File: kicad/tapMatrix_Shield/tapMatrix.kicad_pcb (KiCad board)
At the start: 2 copper layers, 68.6 x 53.3 mm, 29 parts, among them P5 TS_ZIF, P6 LED_MATRIX_HDR, U1 MCP1700T-3302E/MB, U2 MCP4921-E/SN, U3 74LS125, U4 TL072, U5 SD_CARD, U6 DS1307

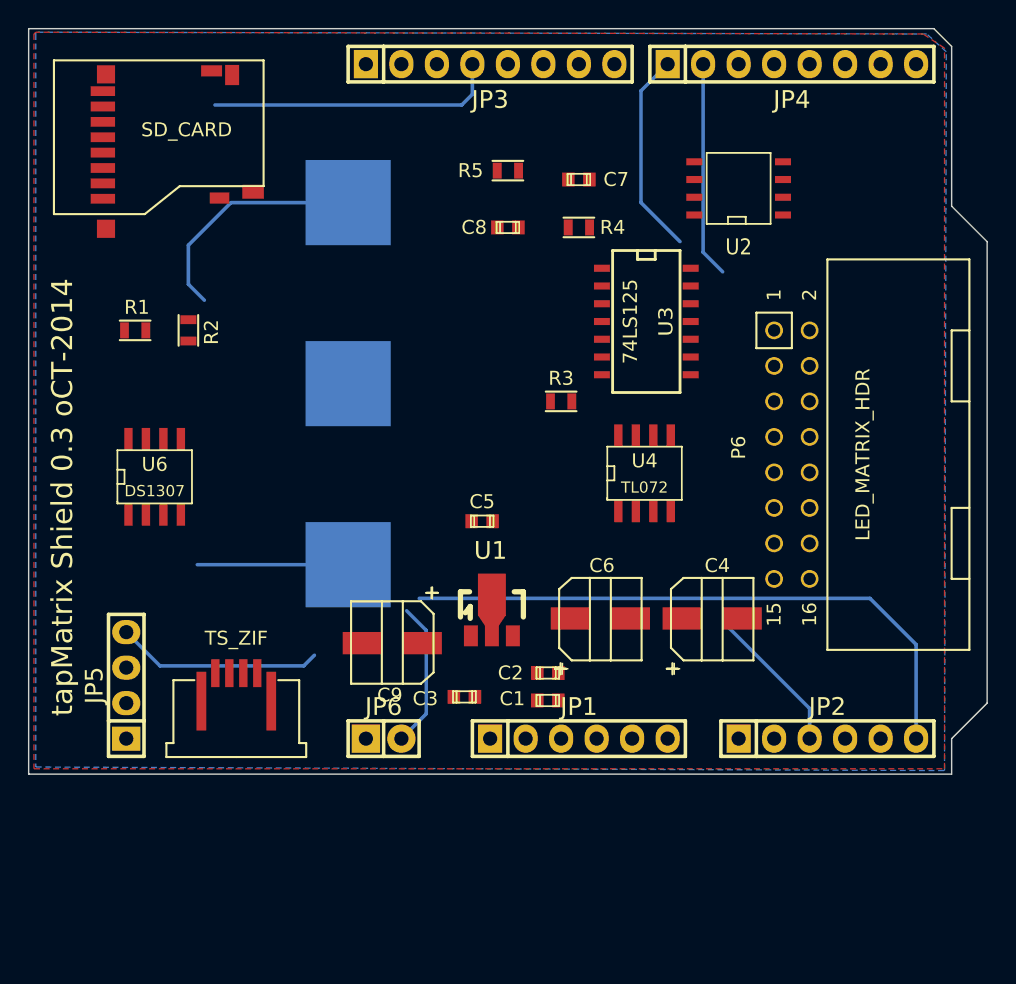
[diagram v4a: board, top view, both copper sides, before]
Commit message: catch up with commits for moving R and C to tapmatrix library
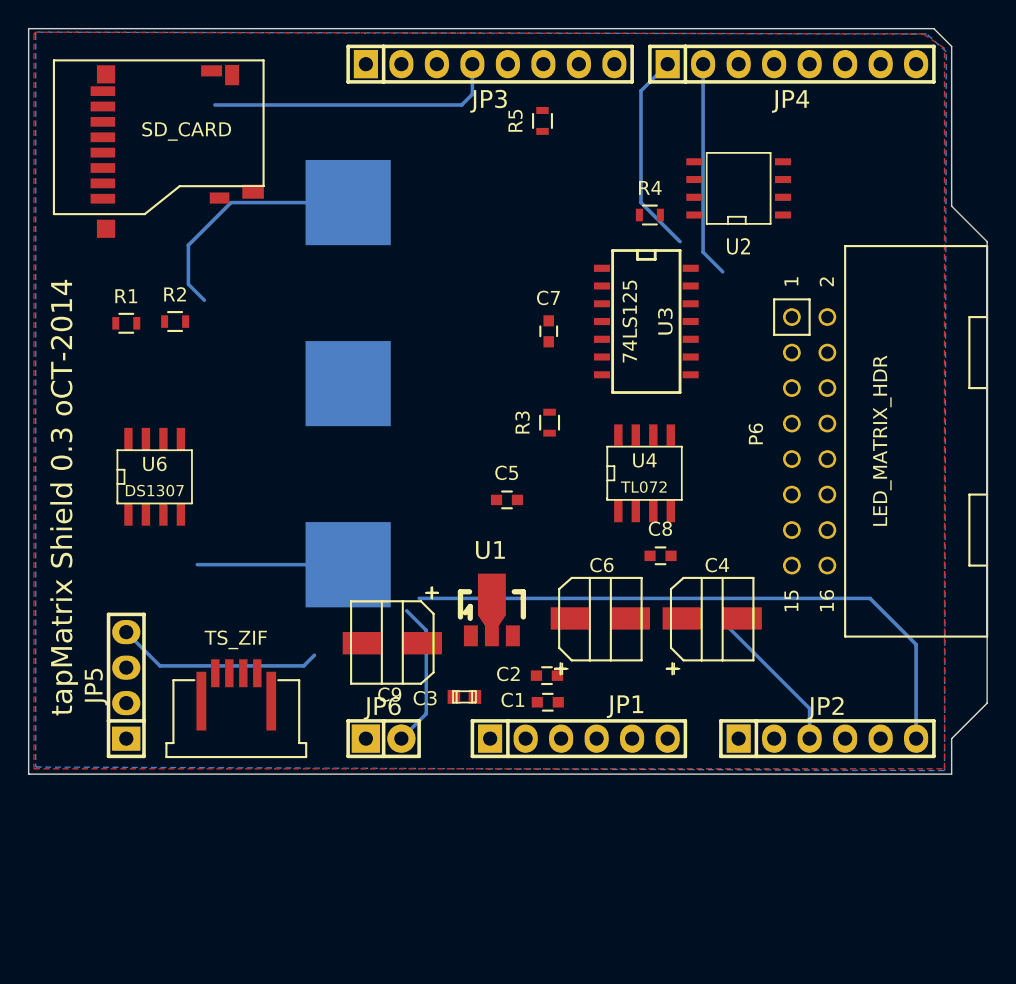
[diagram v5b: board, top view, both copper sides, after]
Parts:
- C1, C2, C5, C7, C8: footprint Capacitors_SMD:c_0603 -> tapmatrix:C_0603
- R1, R2, R3, R4, R5: footprint Resistors_SMD:R_0603 -> tapmatrix:R_0603
- moved C8 25.9 mm to (176.0, 124.1)
- moved C7 11.1 mm to (168.0, 108.0), turned to 270 degrees
- moved R4 5.16 mm to (175.3, 99.7)
- moved R5 4.33 mm to (167.6, 93.0), turned to 90 degrees
- moved C5 2.34 mm to (165.0, 120.1)
- moved R3 1.73 mm to (168.1, 114.6), turned to 90 degrees
- moved P6 1.59 mm to (186.7, 115.9)
- moved R2 1.14 mm to (141.3, 107.3), turned to 0 degrees
- moved R1 0.81 mm to (137.8, 107.4)
- moved C2 0.20 mm to (167.9, 132.7), turned to 180 degrees
- moved C1 0.13 mm to (168.0, 134.6), turned to 180 degrees

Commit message: move pin header footprints to tapmatrix library
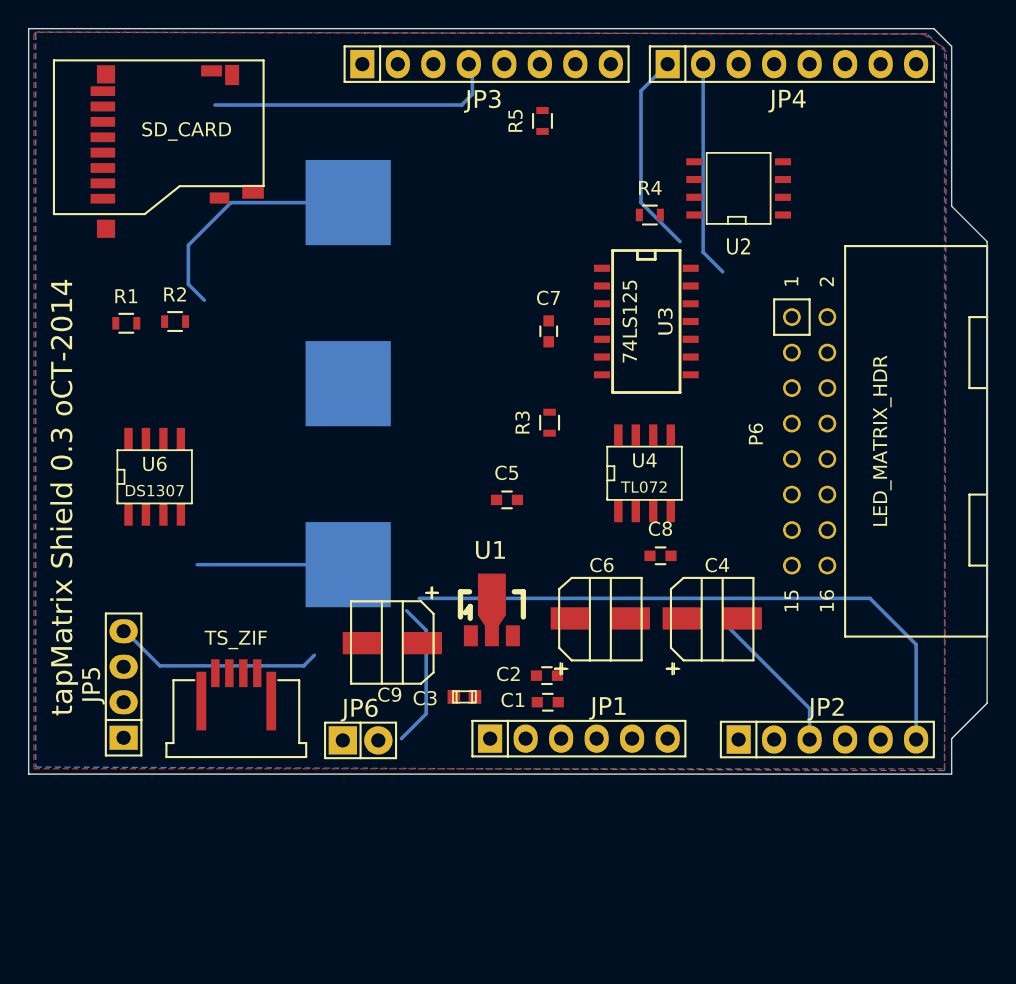
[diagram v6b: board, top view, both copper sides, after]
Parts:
- JP1, JP2: footprint Pin_Headers:Pin_Header_Straight_1x06 -> tapmatrix:Pin_Header_Straight_1x06
- JP3, JP4: footprint Pin_Headers:Pin_Header_Straight_1x08 -> tapmatrix:Pin_Header_Straight_1x08
- JP5: footprint Pin_Headers:Pin_Header_Straight_1x04 -> tapmatrix:Pin_Header_Straight_1x04
- JP6: footprint Pin_Headers:Pin_Header_Straight_1x02 -> tapmatrix:Pin_Header_Straight_1x02
- moved JP6 1.66 mm to (154.6, 137.3)
- moved JP3 0.25 mm to (163.6, 88.9)
- moved JP5 0.20 mm to (137.6, 133.3)
- moved JP2 0.06 mm to (188.0, 137.2)
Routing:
- net Net-(C9-Pad2): track 10.5 -> 0.00 mm
- net (no net): track 0.00 -> 10.5 mm

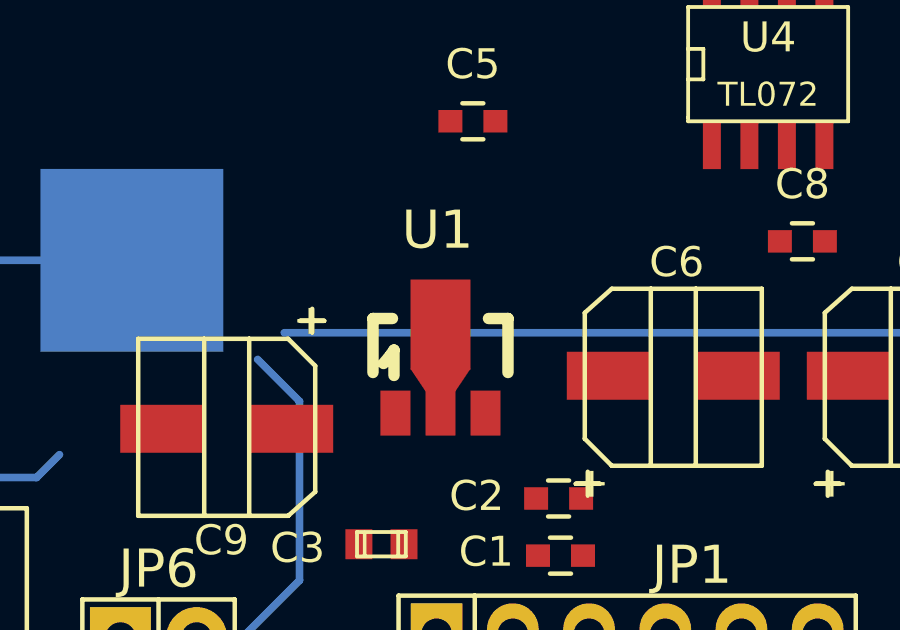
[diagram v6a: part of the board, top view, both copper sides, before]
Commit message: move SOT-89-3 footprint to tapmatrix library
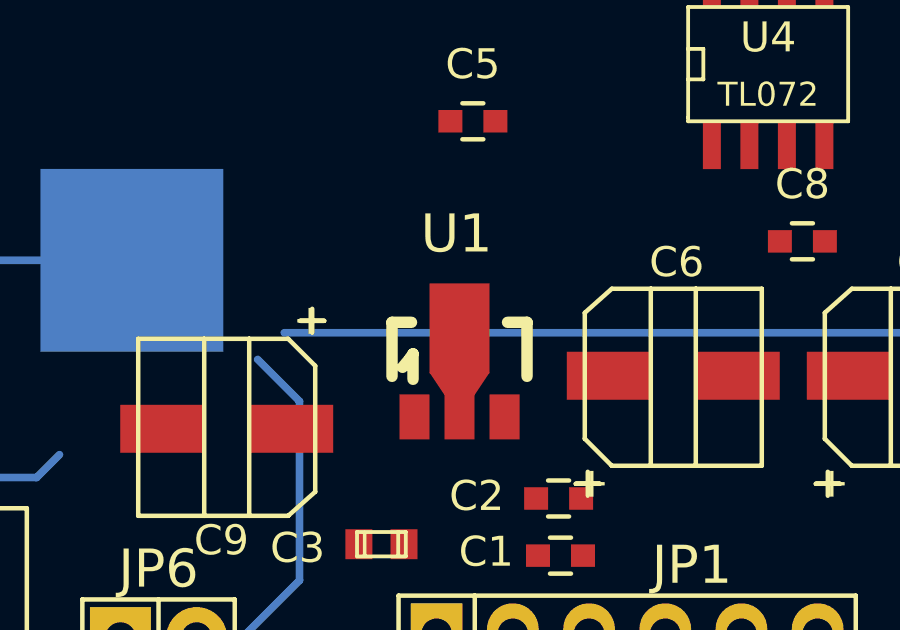
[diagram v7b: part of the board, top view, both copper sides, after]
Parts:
- U1: footprint Housings_SOT-89:SOT89-3_Housing -> tapmatrix:SOT89-3_Housing
- moved U1 0.65 mm to (164.6, 128.1)
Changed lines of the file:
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@@
-    )
-  )
-  (module Housings_SOT-89:SOT89-3_Housing (layer F.Cu)
-    (at 163.957 127.9525)
-    (descr "SOT89-3, Housing,")
-    (tags "SOT89-3, Housing,")
-    (attr smd)
-    (fp_text reference U1 (at -0.09906 -4.24942) (layer F.SilkS)
-      (effects (font (thickness 0.3048)))
-    )
-    (fp_text value MCP1700T-3302E/MB (at -0.20066 4.59994) (layer F.SilkS) hide
-      (effects (font (thickness 0.3048)))
-    )
-    (fp_line (start -1.89992 0.20066) (end -1.651 -0.09906) (layer F.SilkS) (width 0.381))
-    (fp_line (start -1.651 -0.09906) (end -1.5494 -0.24892) (layer F.SilkS) (width 0.381))
-    (fp_line (start -1.5494 -0.24892) (end -1.5494 0.59944) (layer F.SilkS) (width 0.381))
-    (fp_line (start -2.25044 -1.30048) (end -2.25044 0.50038) (layer F.SilkS) (width 0.381))
-    (fp_line (start -2.25044 -1.30048) (end -1.6002 -1.30048) (layer F.SilkS) (width 0.381))
-    (fp_line (start 2.25044 -1.30048) (end 2.25044 0.50038) (layer F.SilkS) (width 0.381))
-    (fp_line (start 2.25044 -1.30048) (end 1.6002 -1.30048) (layer F.SilkS) (width 0.381))
-    (pad 1 smd rect (at -1.50114 1.85166) (size 1.00076 1.50114) (layers F.Cu F.Paste F.Mask)
-      (net 2 GND))
-    (pad 2 smd rect (at 0 1.85166) (size 1.00076 1.50114) (layers F.Cu F.Paste F.Mask)
-      (net 46 +3.3V))
-    (pad 3 smd rect (at 1.50114 1.85166) (size 1.00076 1.50114) (layers F.Cu F.Paste F.Mask)
-      (net 1 +5V))
-    (pad 2 smd rect (at 0 -1.09982) (size 1.99898 2.99974) (layers F.Cu F.Paste F.Mask)
-      (net 46 +3.3V))
-    (pad 2 smd trapezoid (at 0 0.7493 180) (size 1.50114 0.7493) (rect_delta 0 0.50038 ) (layers F.Cu F.Paste F.Mask)
-      (net 46 +3.3V))
-    (model SOT89-3_SOT89-5_Housing_Wings3d_RevA_02Sep2012/SOT89-3_Housing_Faktor03937_RevA_02Sep2012.wrl
-      (at (xyz 0 0 0))
-      (scale (xyz 0.3937000036239624 0.3937000036239624 0.3937000036239624))
-      (rotate (xyz 0 0 0))
     )
   )
@@
       (rotate (xyz 0 0 0))
     )
+  )
+  (module tapmatrix:SOT89-3_Housing (layer F.Cu)
+    (at 164.592 128.0795)
+    (descr "SOT89-3, Housing,")
+    (tags "SOT89-3, Housing,")
+    (attr smd)
+    (fp_text reference U1 (at -0.09906 -4.24942) (layer F.SilkS)
+      (effects (font (thickness 0.3048)))
+    )
+    (fp_text value MCP1700T-3302E/MB (at -0.20066 4.59994) (layer F.SilkS) hide
+      (effects (font (thickness 0.3048)))
+    )
+    (fp_line (start -1.89992 0.20066) (end -1.651 -0.09906) (layer F.SilkS) (width 0.381))
+    (fp_line (start -1.651 -0.09906) (end -1.5494 -0.24892) (layer F.SilkS) (width 0.381))
+    (fp_line (start -1.5494 -0.24892) (end -1.5494 0.59944) (layer F.SilkS) (width 0.381))
+    (fp_line (start -2.25044 -1.30048) (end -2.25044 0.50038) (layer F.SilkS) (width 0.381))
+    (fp_line (start -2.25044 -1.30048) (end -1.6002 -1.30048) (layer F.SilkS) (width 0.381))
+    (fp_line (start 2.25044 -1.30048) (end 2.25044 0.50038) (layer F.SilkS) (width 0.381))
+    (fp_line (start 2.25044 -1.30048) (end 1.6002 -1.30048) (layer F.SilkS) (width 0.381))
+    (pad 1 smd rect (at -1.50114 1.85166) (size 1.00076 1.50114) (layers F.Cu F.Paste F.Mask)
+      (net 2 GND))
+    (pad 2 smd rect (at 0 1.85166) (size 1.00076 1.50114) (layers F.Cu F.Paste F.Mask)
+      (net 46 +3.3V))
+    (pad 3 smd rect (at 1.50114 1.85166) (size 1.00076 1.50114) (layers F.Cu F.Paste F.Mask)
+      (net 1 +5V))
+    (pad 2 smd rect (at 0 -1.09982) (size 1.99898 2.99974) (layers F.Cu F.Paste F.Mask)
+      (net 46 +3.3V))
+    (pad 2 smd trapezoid (at 0 0.7493 180) (size 1.50114 0.7493) (rect_delta 0 0.50038 ) (layers F.Cu F.Paste F.Mask)
+      (net 46 +3.3V))
+    (model SOT89-3_SOT89-5_Housing_Wings3d_RevA_02Sep2012/SOT89-3_Housing_Faktor03937_RevA_02Sep2012.wrl
+      (at (xyz 0 0 0))
+      (scale (xyz 0.3937000036239624 0.3937000036239624 0.3937000036239624))
+      (rotate (xyz 0 0 0))
+    )

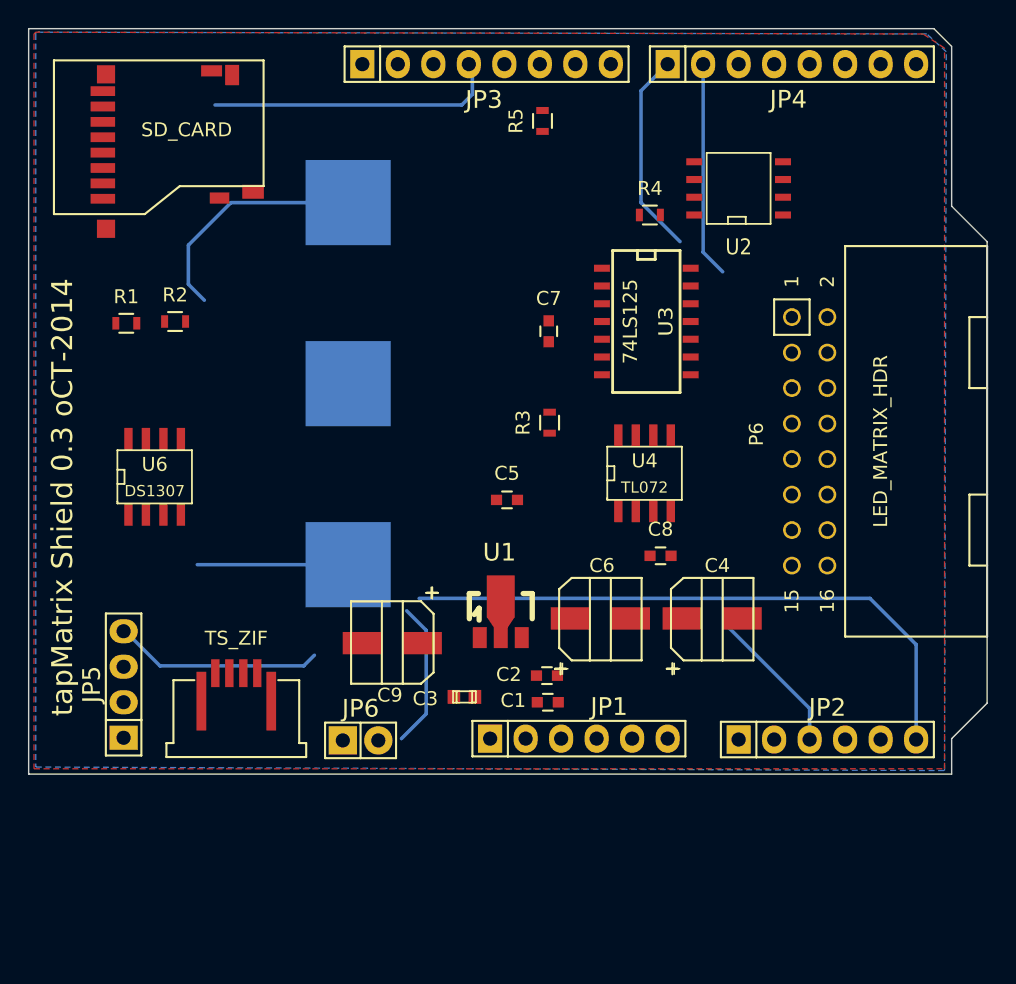
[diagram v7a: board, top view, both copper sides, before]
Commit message: moved SOIC footprints to tapmatrix library
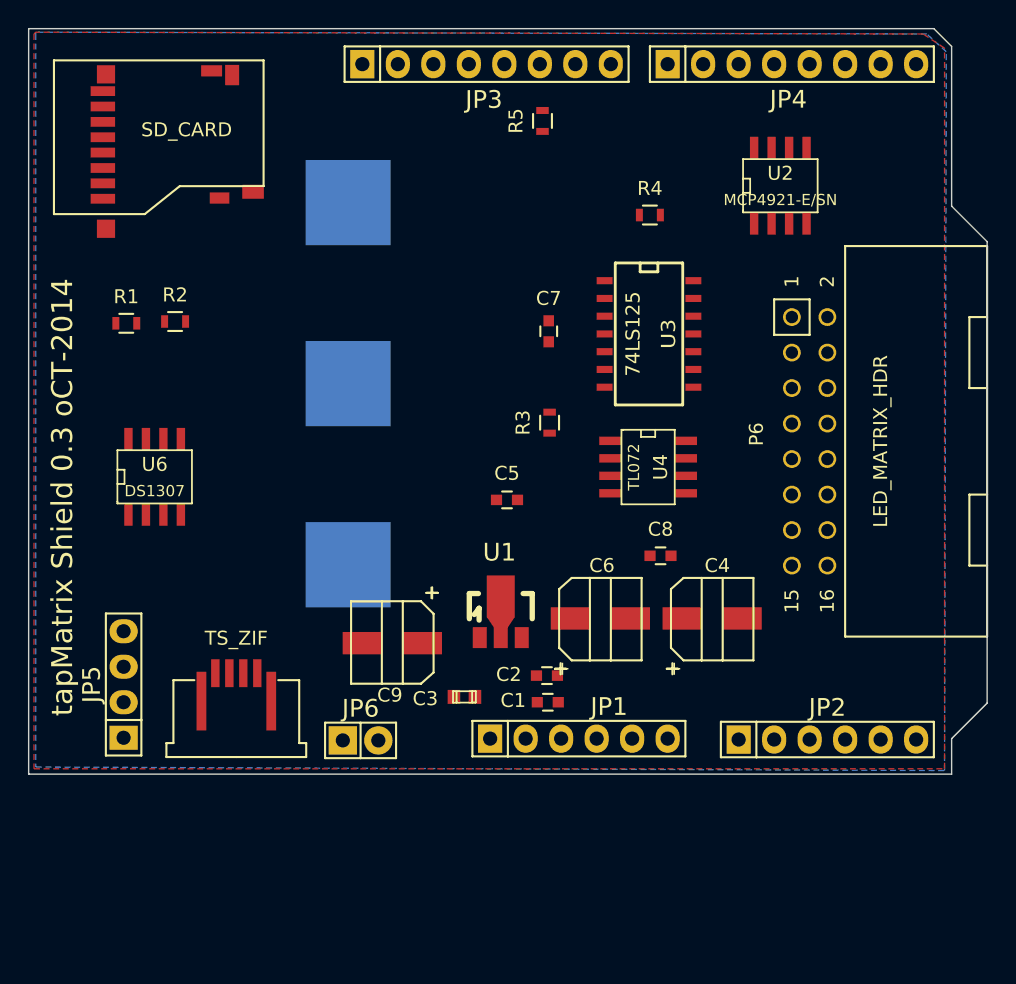
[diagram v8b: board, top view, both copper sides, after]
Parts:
- U2: footprint SMD_Packages:SOIC-8-N -> tapmatrix:SOIC-8_N
- U3: footprint SMD_Packages:SOIC-14_N -> tapmatrix:SOIC-14_N
- U4: footprint Housings_SOIC:SOIC-8_N -> tapmatrix:SOIC-8_N
- moved U2 2.99 mm to (184.6, 97.6), turned to 0 degrees
- moved U3 0.91 mm to (175.3, 108.2)
- moved U4 0.51 mm to (175.1, 117.7), turned to 270 degrees
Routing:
- net /I2C_SCL: track 43.7 -> 0.00 mm
- net Net-(BT1-Pad1): track 29.2 -> 0.00 mm
- net /MISO: track 20.9 -> 0.00 mm
- net /MATRIX_DATA: track 15.4 -> 0.00 mm
- net /YM: track 14.8 -> 0.00 mm
- net /MATRIX_WR: track 14.6 -> 0.00 mm
- net /XP: track 10.8 -> 0.00 mm
- net (no net): track 10.5 -> 0.00 mm
